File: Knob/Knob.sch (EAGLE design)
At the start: 9 parts, among them U1 ATTINY48/88-TQFP, U2 JOYSTICK

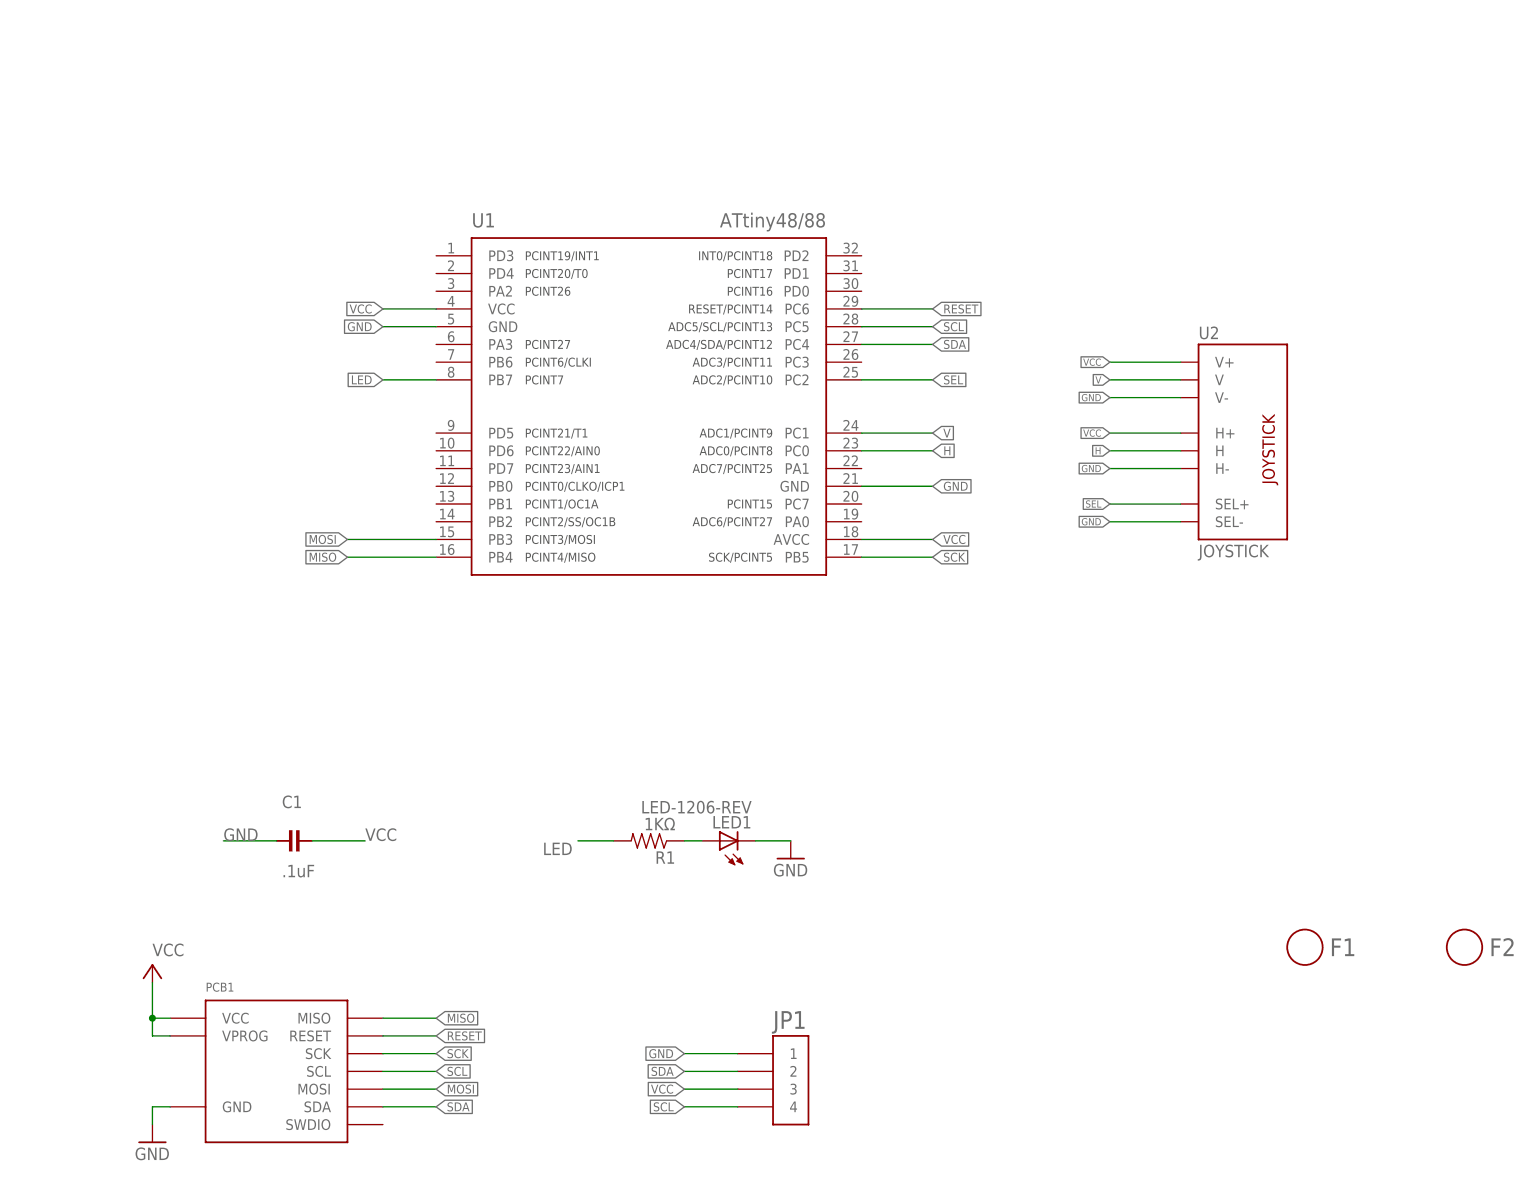
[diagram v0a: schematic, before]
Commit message: Major revision of all boards. Cleaned up old files. Exported BOM csv files for all boards
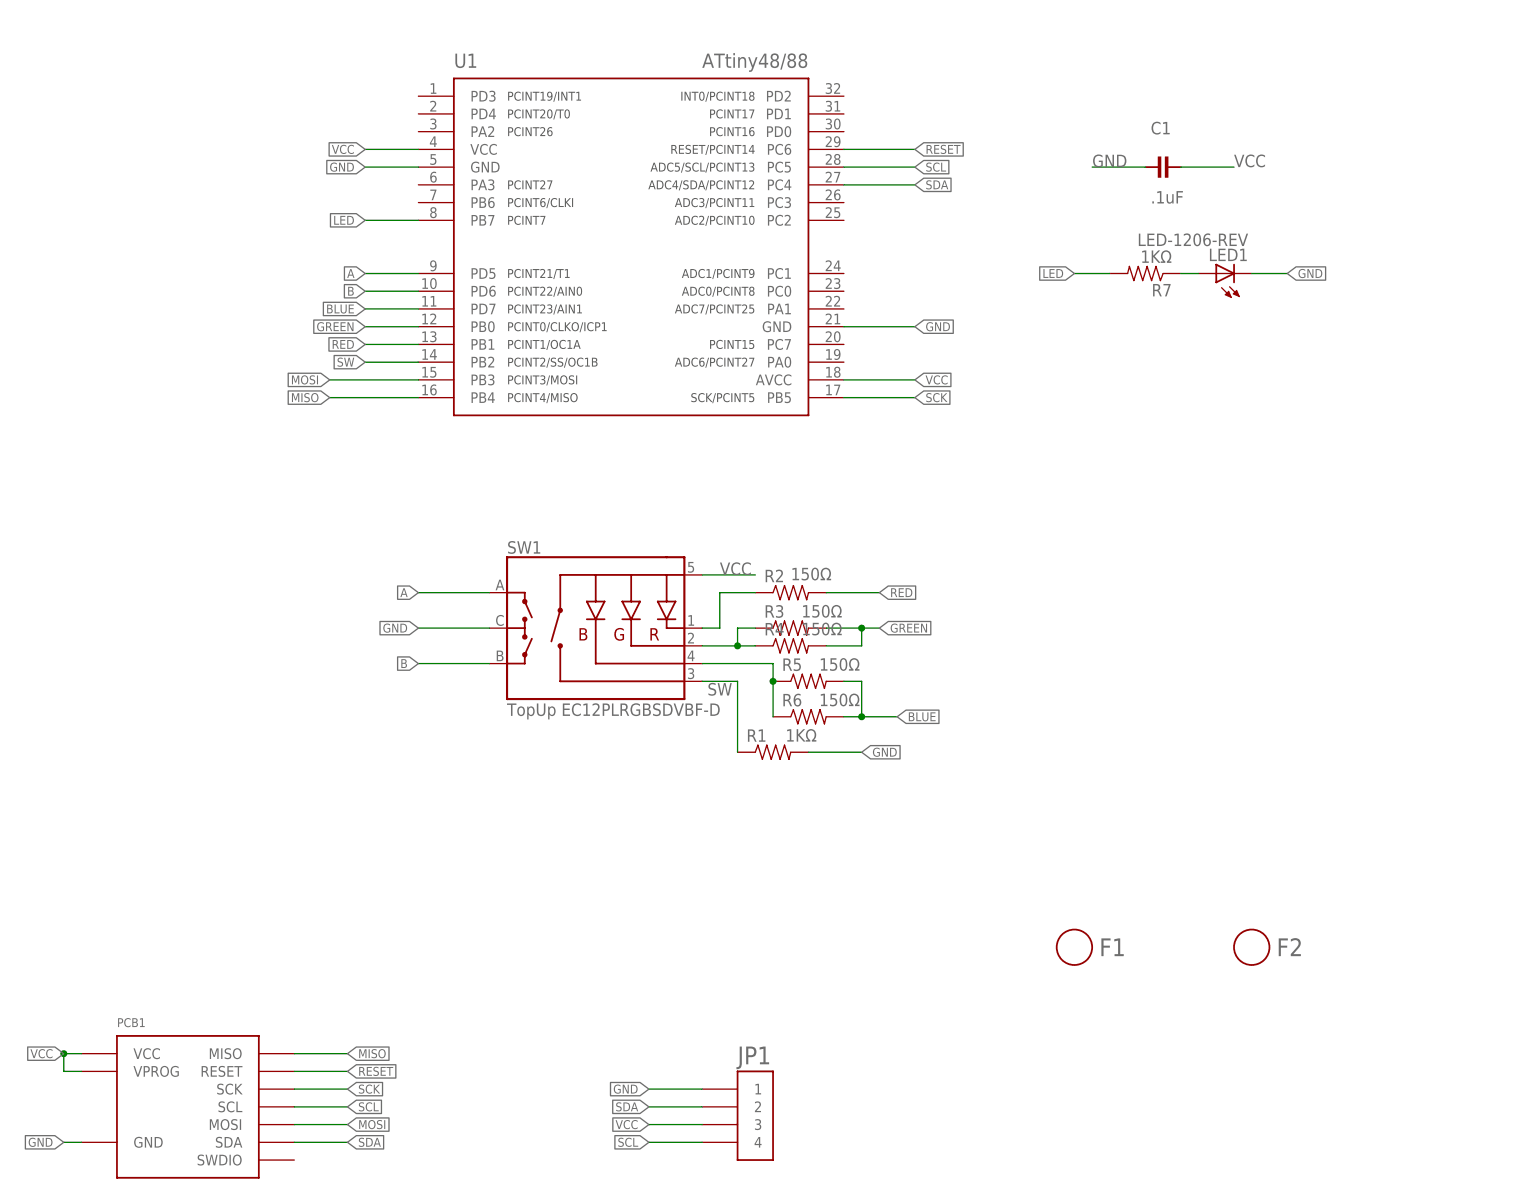
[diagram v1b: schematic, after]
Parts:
- removed U2: JOYSTICK, Modulo:JOYSTICK
- added R2, R3, R4, R5, R6: 150Ω, Modulo:RESISTOR-150Ω
- added R7: 1KΩ, Modulo:RESISTOR-1KΩ
- added SW1: TopUp EC12PLRGBSDVBF-D, Modulo:ENCODER_RGB_CASIDEPADS
- F1, F2: BOM EXCLUDE -> (none)
- PCB1: NOBOM 1 -> (none); PARTNUM Joystick PCB -> Knob PCB
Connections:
- removed net H: U1.PC0, U2.H
- removed net N$1: LED1.A, R1.1
- removed net SEL: U1.PC2, U2.SEL+
- removed net V: U1.PC1, U2.V
- new net A: SW1.A, U1.PD5
- new net B: SW1.B, U1.PD6
- new net BLUE: R5.2, R6.2, U1.PD7
- new net GREEN: R3.2, R4.2, U1.PB0
- new net N$4: R2.1, SW1.-R
- new net N$5: R3.1, R4.1, SW1.-G
- new net N$6: R5.1, R6.1, SW1.-B
- new net N$7: LED1.A, R7.1
- new net RED: R2.2, U1.PB1
- new net SW: R1.1, SW1.SW, U1.PB2
- net GND: now also R1.2, SW1.C; no longer U2.H-, U2.SEL-, U2.V-
- net LED: now also R7.2; no longer R1.2
- net VCC: now also SW1.+; no longer U2.H+, U2.V+
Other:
- moved on the sheet: C1, F1, F2, JP1, LED1, PCB1, R1, U1

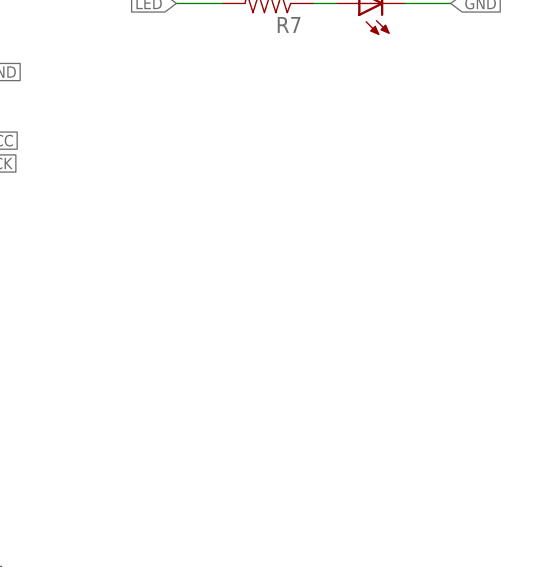
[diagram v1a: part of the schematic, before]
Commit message: Added knob cap BOM item
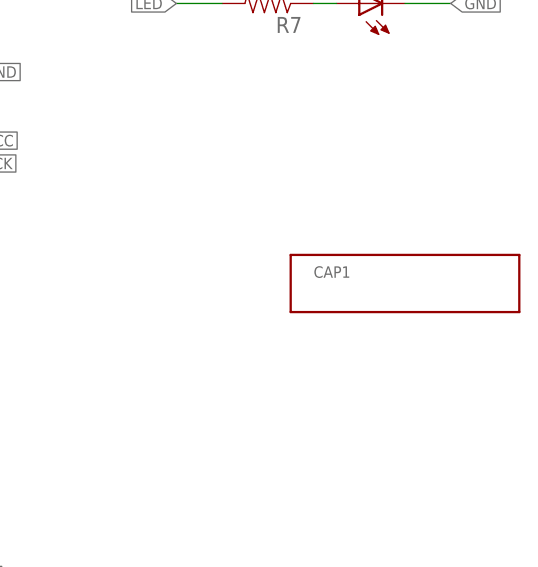
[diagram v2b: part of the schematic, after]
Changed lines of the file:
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@@
 <part name="R5" library="Modulo" deviceset="RESISTOR" device="-150Ω" value="150Ω"/>
 <part name="R4" library="Modulo" deviceset="RESISTOR" device="-150Ω" value="150Ω"/>
+<part name="CAP1" library="Modulo" deviceset="BOM_ITEM" device="">
+<attribute name="PARTNUM" value="Knob Cap"/>
+</part>
 </parts>
 <sheets>
@@
 <attribute name="VALUE" x="125.984" y="90.424" size="1.778" layer="96"/>
 </instance>
+<instance part="CAP1" gate="G$1" x="182.88" y="109.22">
+<attribute name="PARTNUM" x="182.88" y="109.22" size="1.778" layer="96" display="off"/>
+</instance>
 </instances>

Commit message: Check point of current PCB designs. Among other things I think this change includes rewiring of programming lines on many of the boards,.
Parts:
- removed U1: ATTINY48/88-TQFP, Modulo:ATTINY48/88-TQFP
- added R8, R9: 150Ω, Modulo:RESISTOR-150Ω
- added U2: ATTINY841, Modulo:ATTINY841
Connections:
- removed net LED: R7.2, U1.PB7
- removed net MISO: PCB1.MISO, U1.PB4
- removed net MOSI: PCB1.MOSI, U1.PB3
- removed net SCK: PCB1.SCK, U1.PB5
- new net MISO/LED: PCB1.MISO, R7.2, U2.PA5
- new net SCL/SCK: R8.2, U2.PA4
- new net SDA/MOSI: R9.2, U2.PA6
- net A: now also U2.PB1; no longer U1.PD5
- net B: now also U2.PB0; no longer U1.PD6
- net BLUE: now also U2.PB2; no longer U1.PD7
- net GND: now also U2.GND; no longer U1.GND, U1.GND@1
- net GREEN: now also U2.PA7; no longer U1.PB0
- net RED: now also U2.PA1; no longer U1.PB1
- net RESET: now also U2.PB3; no longer U1.PC6
- net SCL: now also PCB1.SCK, R8.1; no longer U1.PC5
- net SDA: now also PCB1.MOSI, R9.1; no longer U1.PC4
- net SW: now also U2.PA2; no longer U1.PB2
- net VCC: now also U2.VCC; no longer U1.AVCC, U1.VCC
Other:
- moved on the sheet: R1, R2, R3, R4, R5, R6, SW1
